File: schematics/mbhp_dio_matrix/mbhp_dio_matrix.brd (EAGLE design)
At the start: 80 x 40 mm, 22 parts, among them IC1 74HC595, IC2 74HC595, IC3 74HC165, IC4 74HC165

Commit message: mbhp_dio_matrix.brd finalized
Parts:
- moved RN1 1.27 mm to (21.0, 34.9)
- moved RN3 1.27 mm to (50.2, 34.9)
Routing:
- net RC: track 180.5 -> 156.0 mm
- net SC: track 175.1 -> 170.5 mm
- net S$1: track 65.8 -> 62.4 mm
- net S$19: track 33.5 -> 30.3 mm
- net S$8: track 31.9 -> 29.5 mm
- net S$16: track 31.9 -> 29.5 mm
- net S$9: track 37.7 -> 35.7 mm
- net VDD: track 168.9 -> 166.9 mm
- net S$17: track 37.5 -> 35.7 mm
- net S$20: track 33.2 -> 31.4 mm
- net S$7: track 20.7 -> 19.5 mm
- net S$15: track 20.7 -> 19.5 mm
- net GND: track 192.6 -> 193.6 mm, vias 4 -> 5
- net S$42: track 55.2 -> 54.3 mm
- net S$10: track 44.2 -> 43.4 mm
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- added copper zone on layer 16, net GND
- removed copper zone on layer 16, net S$21

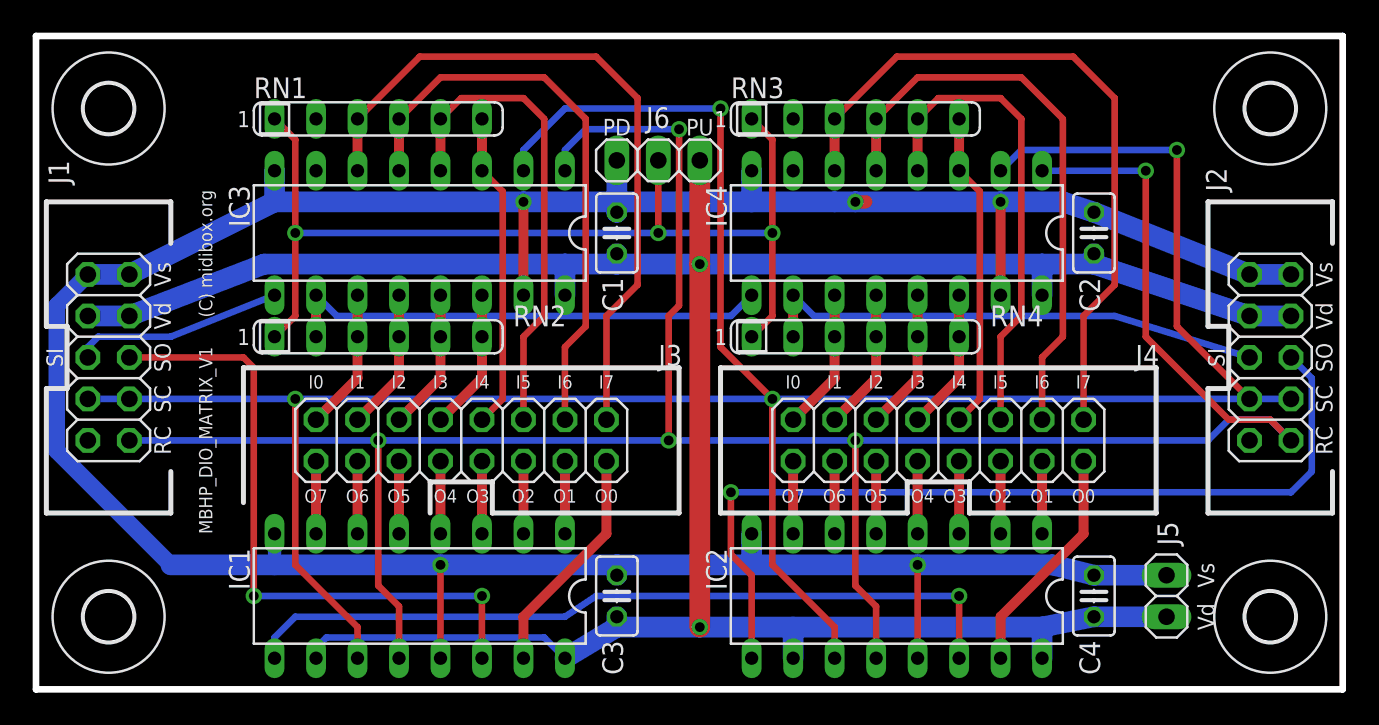
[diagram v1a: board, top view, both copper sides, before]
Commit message: mbhp_dio_matrix.brd: modified as requested by Olimex
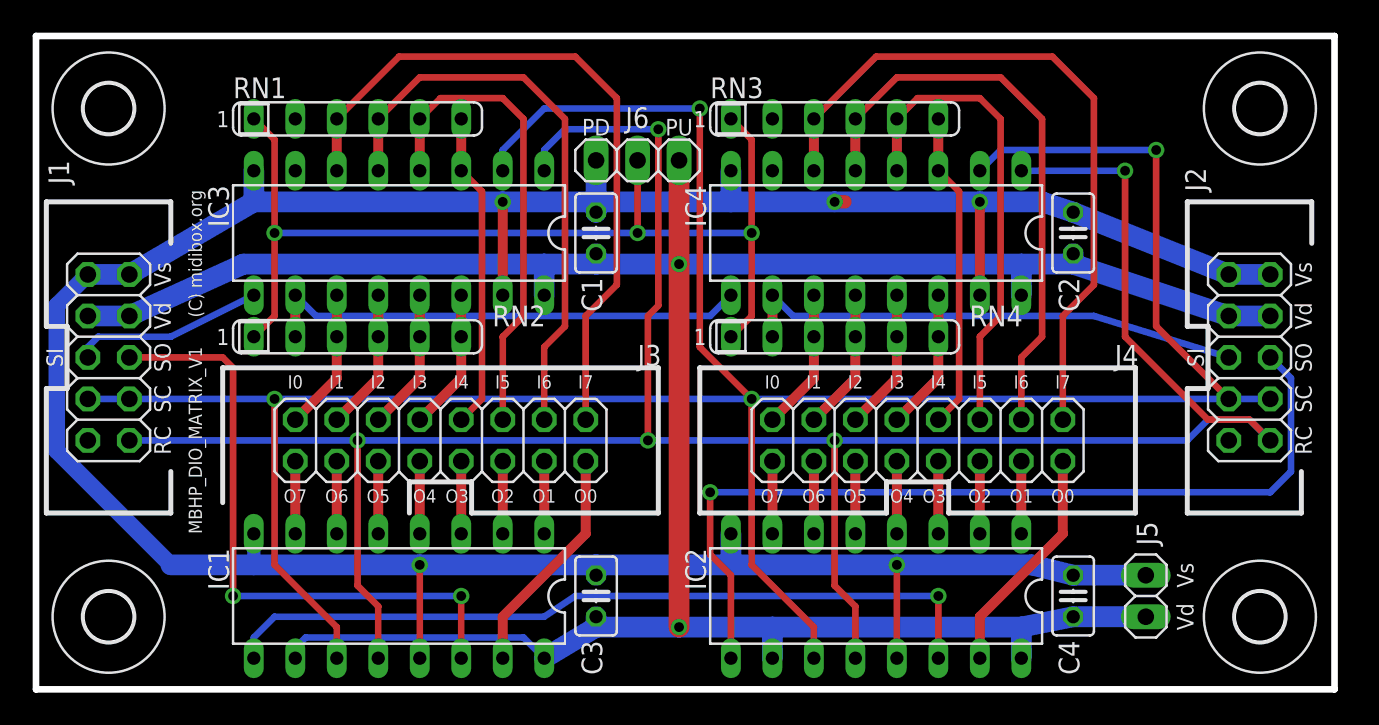
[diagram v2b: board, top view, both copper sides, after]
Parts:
- moved J5 1.27 mm to (67.9, 5.71)
- moved C1 1.27 mm to (34.3, 27.9)
- moved C3 1.27 mm to (34.3, 5.71)
- moved J6 1.27 mm to (36.8, 32.4)
- moved IC1 1.27 mm to (22.2, 5.71)
- moved IC3 1.27 mm to (22.2, 27.9)
- moved J3 1.27 mm to (24.8, 15.2)
- moved RN1 1.27 mm to (19.7, 34.9)
- moved RN2 1.27 mm to (19.7, 21.6)
- moved C2 1.27 mm to (63.5, 27.9)
- moved C4 1.27 mm to (63.5, 5.71)
- moved IC2 1.27 mm to (51.4, 5.71)
- moved IC4 1.27 mm to (51.4, 27.9)
- moved J2 1.27 mm to (74.3, 20.3)
- moved J4 1.27 mm to (54.0, 15.2)
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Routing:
- net GND: track 193.6 -> 191.2 mm
- net RC: track 156.0 -> 154.7 mm
- net SO: track 39.6 -> 38.4 mm
- net SC: track 170.5 -> 169.2 mm
- net VDD: track 166.9 -> 165.8 mm
- net SI: track 12.8 -> 11.7 mm
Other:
- board size 80 x 40 mm -> 79.5 x 40 mm
